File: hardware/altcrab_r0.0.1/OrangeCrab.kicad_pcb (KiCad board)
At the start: 6 copper layers, 50.8 x 22.9 mm, 163 parts, among them J1 Conn_01x12_Male, J2 Conn_01x16_Male, J3 USB_C_Receptacle_USB2.0, J4 MicroSd, J5 JST, J6 Conn_01x05_Male, SW1 SW_Push, U1 TLV62569DRL, U10 NCP115-2.5, U2 TLV62569DRL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

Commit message: kicad 9 upgrade
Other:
- net class DDR3_CTRL_LM1.0 removed
- net class DDR3_DQS0_LM1.0 removed
- net class DDR3_DQS1_LM1.0 removed
- net class DDR_CLK_LM1.0 removed
- net class Default removed

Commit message: after update from schematic
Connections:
- D2 pad 4: Net-(D2-Pad4) -> unconnected-(D2-BK-Pad4)
- J3 pad A8: Net-(J3-PadA8) -> unconnected-(J3-SBU1-PadA8)
- J3 pad B8: Net-(J3-PadB8) -> unconnected-(J3-SBU2-PadB8)
- U1 pad 6: Net-(U1-Pad6) -> unconnected-(U1-NC-Pad6)
- U2 pad 6: Net-(U2-Pad6) -> unconnected-(U2-NC-Pad6)
- U3 pad A10: Net-(U3-PadA10) -> unconnected-(U3A-PT27B/PCLKC0_1-PadA10)
- U3 pad A11: Net-(U3-PadA11) -> unconnected-(U3A-PT27A/PCLKT0_1-PadA11)
- U3 pad B11: Net-(U3-PadB11) -> unconnected-(U3A-PT4A-PadB11)
- U3 pad C11: Net-(U3-PadC11) -> unconnected-(U3A-PT4B-PadC11)
- U3 pad H18: Net-(U3-PadH18) -> unconnected-(U3E-PL38D-PadH18)
- U3 pad R16: Net-(U3-PadR16) -> unconnected-(U3G-PB18A/WRITEN-PadR16)
- U3 pad U15: Net-(U3-PadU15) -> unconnected-(U3H-DONE-PadU15)
- U3 pad V11: Net-(U3-PadV11) -> unconnected-(U3H-RESERVED-PadV11)
- U3 pad V12: Net-(U3-PadV12) -> unconnected-(U3H-RESERVED-PadV12)
- U3 pad V16: Net-(U3-PadV16) -> unconnected-(U3H-INITN-PadV16)
- U3 pad V2: Net-(U3-PadV2) -> unconnected-(U3H-RESERVED-PadV2)
- U3 pad V3: Net-(U3-PadV3) -> unconnected-(U3H-RESERVED-PadV3)
- U7 pad 6: Net-(U7-Pad6) -> unconnected-(U7-NC-Pad6)

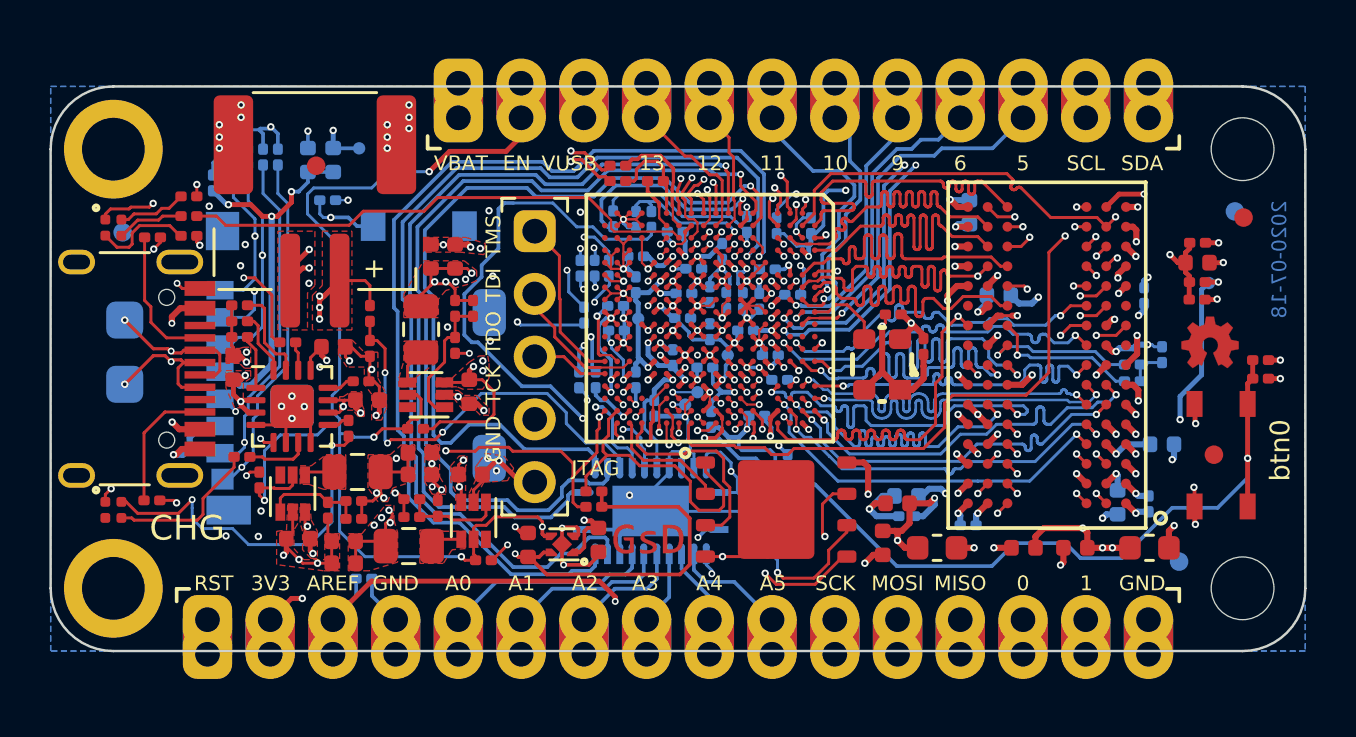
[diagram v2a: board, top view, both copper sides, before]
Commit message: update pcb from schematic after footprint changes
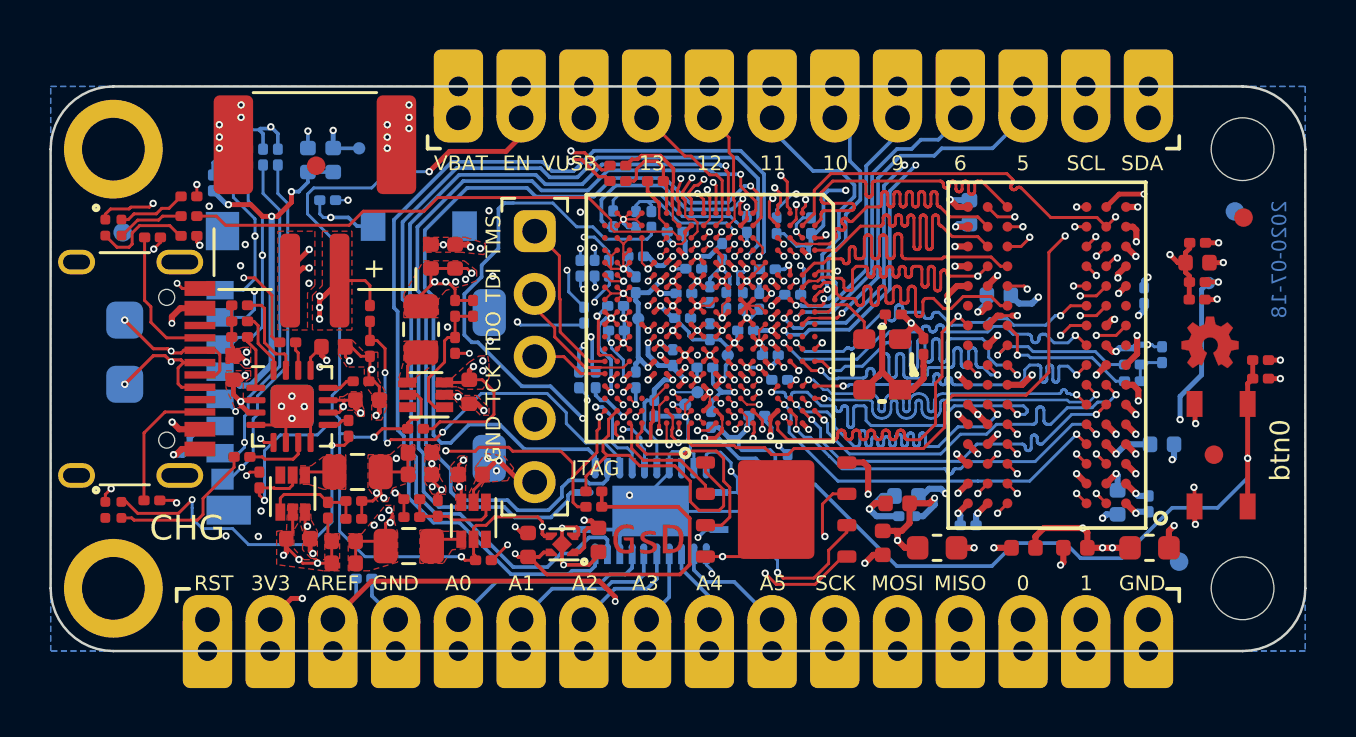
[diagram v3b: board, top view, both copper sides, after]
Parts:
- J1: footprint gkl_conn:Feather_PinHeader_1x12 -> w531t4_altcrab_footprints:Feather_PinHeader_1x12 _ castellated
- J2: footprint gkl_conn:Feather_PinHeader_1x16 -> w531t4_altcrab_footprints:Feather_PinHeader_1x16_castellated
